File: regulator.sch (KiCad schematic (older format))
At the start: 25 parts, among them IC1 PIC12F675-I/P, Q1 PN2222A, Q2 2N2907A, Q3 BUK9511-55A (Logic Level), Q4 PN2222A, Q5 BUK9511-55A (Logic Level), U1 LM7805

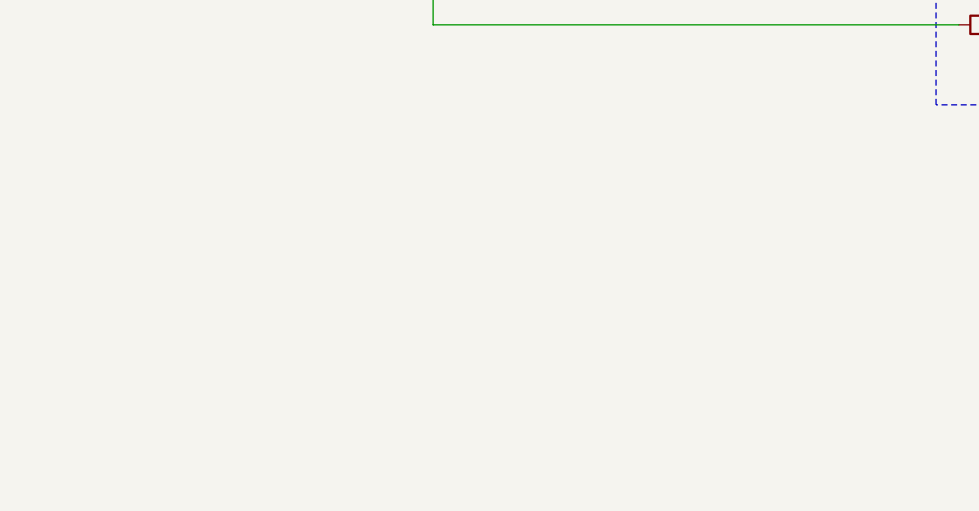
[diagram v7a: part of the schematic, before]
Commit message: Change over voltage reduction parameter. Update Schematic.
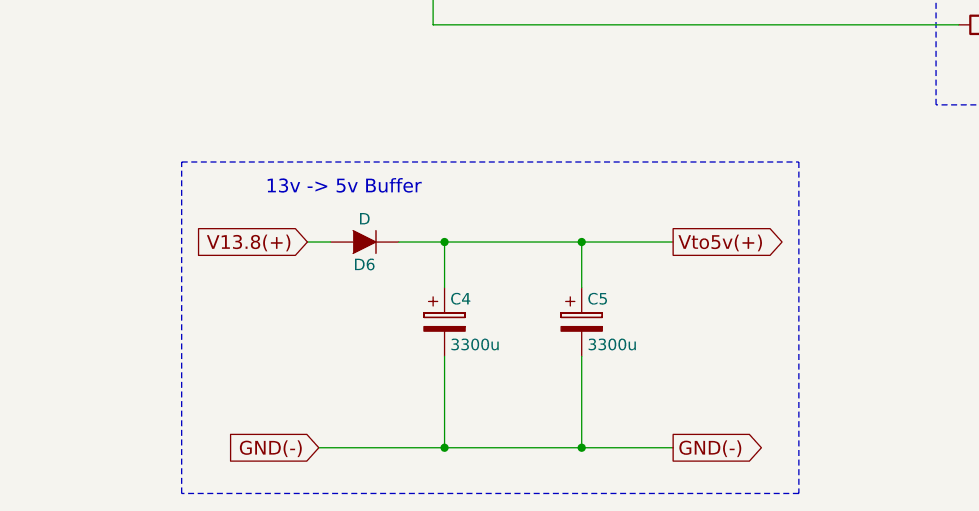
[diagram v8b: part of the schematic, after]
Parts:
- added C4, C5: 3300u, symbol CP
- added D6: D, symbol D
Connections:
- new net GND(-): C4.2, C5.2
- new net V13.8(+): D6.2 (A)
- new net Vto5v(+): C4.1, C5.1, D6.1 (K)
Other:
- note added: "13v -> 5v Buffer"
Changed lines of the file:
@@
 Sheet 1 1
 Title "PWM Regulator v3"
-Date "2015-07-30"
-Rev "1.2j"
+Date "2015-08-03"
+Rev "1.2k"
 Comp ""
 Comment1 ""
@@
 Text Notes 3750 3950 2    60   ~ 0
 GP3 (GND) = 5v\nGP4 (GND) = Check Charging
-Wire Wire Line
-	4800 3700 4800 3900
-Wire Wire Line
-	2250 3700 2250 3350
-Connection ~ 4800 3700
-Connection ~ 4800 1850
-Wire Wire Line
-	6600 3700 6600 2550
-Wire Wire Line
-	6600 2250 6600 1850
-Connection ~ 6600 1850
-Wire Wire Line
-	7400 1850 8650 1850
-Connection ~ 2250 3700
-Wire Wire Line
-	1750 2750 2250 2750
-Wire Wire Line
-	1900 3300 1900 3700
-Connection ~ 1900 3700
-Wire Wire Line
-	7550 1850 7550 2200
-Connection ~ 7550 1850
-Wire Wire Line
-	7550 3700 7550 2500
-Connection ~ 6600 3700
-Wire Wire Line
-	8000 1850 8000 2350
-Connection ~ 8000 1850
-Wire Wire Line
-	8000 2650 8000 2900
-Connection ~ 7550 3700
-Wire Wire Line
-	3850 2750 4050 2750
-Wire Wire Line
-	4450 3400 7750 3400
-Wire Wire Line
-	7750 3400 7750 2800
-Wire Wire Line
-	7750 2800 8000 2800
-Connection ~ 8000 2800
-Wire Wire Line
-	8150 3700 8150 3150
-Connection ~ 8150 3700
-Wire Wire Line
-	5200 2450 5200 3000
-Wire Wire Line
-	3850 2850 4450 2850
-Wire Wire Line
-	4450 2850 4450 3100
-Wire Wire Line
-	4650 2400 4650 2550
-Wire Wire Line
-	4650 2100 4650 2050
-Wire Wire Line
-	4250 2050 6050 2050
-Wire Wire Line
-	4750 2450 4650 2450
-Connection ~ 4650 2450
-Wire Wire Line
-	4650 3700 4650 2950
-Connection ~ 4650 3700
-Wire Wire Line
-	5050 2450 5200 2450
-Connection ~ 5200 2550
-Wire Wire Line
-	6050 2900 6050 3200
-Wire Wire Line
-	5800 2750 5800 2150
-Connection ~ 4650 2050
-Wire Wire Line
-	6050 2050 6050 2600
-Connection ~ 5500 2050
-Wire Wire Line
-	5500 2050 5500 2350
-Wire Wire Line
-	6200 3200 6200 1850
-Connection ~ 6200 1850
-Wire Wire Line
-	1100 3700 8650 3700
-Wire Wire Line
-	1900 2050 1900 3000
-Connection ~ 1900 2750
-Wire Wire Line
-	5500 2750 5500 2800
-Wire Wire Line
-	5500 3200 6200 3200
-Connection ~ 6050 3200
-Wire Wire Line
-	5800 2750 5500 2750
-Wire Wire Line
-	6550 1850 6800 1850
-Wire Wire Line
-	6000 1850 6250 1850
-Wire Wire Line
-	950  1850 950  2750
-Wire Wire Line
-	4800 1500 4800 1850
-Wire Wire Line
-	3900 2950 3850 2950
-Wire Wire Line
-	4200 2950 4250 2950
-Wire Wire Line
-	4250 2950 4250 3250
-Wire Wire Line
-	4250 3650 4250 3700
-Connection ~ 4250 3700
-Wire Wire Line
-	1900 2050 3950 2050
-Wire Wire Line
-	2700 1850 5600 1850
-Wire Wire Line
-	2400 1850 950  1850
-Wire Wire Line
-	1350 1500 4800 1500
-Wire Wire Line
-	3650 2350 3850 2350
-Wire Wire Line
-	3850 2350 3850 3050
-Wire Wire Line
-	3350 2350 3200 2350
-Wire Wire Line
-	3200 2350 3200 2050
-Connection ~ 3200 2050
-Wire Wire Line
-	3850 3250 4000 3250
 $Comp
 L R R7
@@
 	0    -1   -1   0
 $EndComp
-Wire Wire Line
-	6300 4700 4000 4700
-Wire Wire Line
-	4000 4700 4000 3250
 $Comp
 L Q_NMOS_GDS-RESCUE-regulator Q5
@@
 	1    0    0    -1
 $EndComp
-Wire Wire Line
-	6700 4700 6600 4700
-Wire Notes Line
-	8350 4300 8350 5050
-Wire Notes Line
-	8350 5050 6200 5050
-Wire Notes Line
-	6200 5050 6200 4300
-Wire Notes Line
-	6200 4300 8350 4300
 Text Notes 6250 4400 0    60   ~ 0
 Replace D1, PWM Sync
 Text Notes 2600 4250 0    60   ~ 0
 Output 2A -> C2 > 420uF
+$Comp
+L CP C4
+U 1 1 55BEEF2F
+P 4050 6000
+F 0 "C4" H 4075 6100 50  0000 L CNN
+F 1 "3300u" H 4075 5900 50  0000 L CNN
+F 2 "" H 4088 5850 30  0000 C CNN
+F 3 "" H 4050 6000 60  0000 C CNN
+	1    4050 6000
+	1    0    0    -1
+$EndComp
+$Comp
+L CP C5
+U 1 1 55BEF2D6
+P 4650 6000
+F 0 "C5" H 4675 6100 50  0000 L CNN
+F 1 "3300u" H 4675 5900 50  0000 L CNN
+F 2 "" H 4688 5850 30  0000 C CNN
+F 3 "" H 4650 6000 60  0000 C CNN
+	1    4650 6000
+	1    0    0    -1
+$EndComp
+$Comp
+L D D6
+U 1 1 55BEF35E
+P 3700 5650
+F 0 "D6" H 3700 5750 50  0000 C CNN
+F 1 "D" H 3700 5550 50  0000 C CNN
+F 2 "" H 3700 5650 60  0000 C CNN
+F 3 "" H 3700 5650 60  0000 C CNN
+	1    3700 5650
+	-1   0    0    1
+$EndComp
+Text GLabel 3450 5650 0    60   Input ~ 0
+V13.8(+)
+Text GLabel 3500 6550 0    60   Input ~ 0
+GND(-)
+Text GLabel 5050 6550 2    60   Output ~ 0
+GND(-)
+Text GLabel 5050 5650 2    60   Output ~ 0
+Vto5v(+)
+Wire Wire Line
+	4800 3700 4800 3900
+Wire Wire Line
+	2250 3700 2250 3350
+Connection ~ 4800 3700
+Connection ~ 4800 1850
+Wire Wire Line
+	6600 3700 6600 2550
+Wire Wire Line
+	6600 2250 6600 1850
+Connection ~ 6600 1850
+Wire Wire Line
+	7400 1850 8650 1850
+Connection ~ 2250 3700
+Wire Wire Line
+	1750 2750 2250 2750
+Wire Wire Line
+	1900 3300 1900 3700
+Connection ~ 1900 3700
+Wire Wire Line
+	7550 1850 7550 2200
+Connection ~ 7550 1850
+Wire Wire Line
+	7550 3700 7550 2500
+Connection ~ 6600 3700
+Wire Wire Line
+	8000 1850 8000 2350
+Connection ~ 8000 1850
+Wire Wire Line
+	8000 2650 8000 2900
+Connection ~ 7550 3700
+Wire Wire Line
+	3850 2750 4050 2750
+Wire Wire Line
+	4450 3400 7750 3400
+Wire Wire Line
+	7750 3400 7750 2800
+Wire Wire Line
+	7750 2800 8000 2800
+Connection ~ 8000 2800
+Wire Wire Line
+	8150 3700 8150 3150
+Connection ~ 8150 3700
+Wire Wire Line
+	5200 2450 5200 3000
+Wire Wire Line
+	3850 2850 4450 2850
+Wire Wire Line
+	4450 2850 4450 3100
+Wire Wire Line
+	4650 2400 4650 2550
+Wire Wire Line
+	4650 2100 4650 2050
+Wire Wire Line
+	4250 2050 6050 2050
+Wire Wire Line
+	4750 2450 4650 2450
+Connection ~ 4650 2450
+Wire Wire Line
+	4650 3700 4650 2950
+Connection ~ 4650 3700
+Wire Wire Line
+	5050 2450 5200 2450
+Connection ~ 5200 2550
+Wire Wire Line
+	6050 2900 6050 3200
+Wire Wire Line
+	5800 2750 5800 2150
+Connection ~ 4650 2050
+Wire Wire Line
+	6050 2050 6050 2600
+Connection ~ 5500 2050
+Wire Wire Line
+	5500 2050 5500 2350
+Wire Wire Line
+	6200 3200 6200 1850
+Connection ~ 6200 1850
+Wire Wire Line
+	1100 3700 8650 3700
+Wire Wire Line
+	1900 2050 1900 3000
+Connection ~ 1900 2750
+Wire Wire Line
+	5500 2750 5500 2800
+Wire Wire Line
+	5500 3200 6200 3200
+Connection ~ 6050 3200
+Wire Wire Line
+	5800 2750 5500 2750
+Wire Wire Line
+	6550 1850 6800 1850
+Wire Wire Line
+	6000 1850 6250 1850
+Wire Wire Line
+	950  1850 950  2750
+Wire Wire Line
+	4800 1500 4800 1850
+Wire Wire Line
+	3900 2950 3850 2950
+Wire Wire Line
+	4200 2950 4250 2950
+Wire Wire Line
+	4250 2950 4250 3250
+Wire Wire Line
+	4250 3650 4250 3700
+Connection ~ 4250 3700
+Wire Wire Line
+	1900 2050 3950 2050
+Wire Wire Line
+	2700 1850 5600 1850
+Wire Wire Line
+	2400 1850 950  1850
+Wire Wire Line
+	1350 1500 4800 1500
+Wire Wire Line
+	3650 2350 3850 2350
+Wire Wire Line
+	3850 2350 3850 3050
+Wire Wire Line
+	3350 2350 3200 2350
+Wire Wire Line
+	3200 2350 3200 2050
+Connection ~ 3200 2050
+Wire Wire Line
+	3850 3250 4000 3250
+Wire Wire Line
+	6300 4700 4000 4700
+Wire Wire Line
+	4000 4700 4000 3250
+Wire Wire Line
+	6700 4700 6600 4700
+Wire Notes Line
+	8350 4300 8350 5050
+Wire Notes Line
+	8350 5050 6200 5050
+Wire Notes Line
+	6200 5050 6200 4300
+Wire Notes Line
+	6200 4300 8350 4300
+Wire Wire Line
+	3450 5650 3550 5650
+Wire Wire Line
+	3850 5650 5050 5650
+Wire Wire Line
+	3500 6550 5050 6550
+Wire Wire Line
+	4050 6150 4050 6550
+Connection ~ 4050 6550
+Wire Wire Line
+	4050 5850 4050 5650
+Connection ~ 4050 5650
+Wire Wire Line
+	4650 6150 4650 6550
+Connection ~ 4650 6550
+Wire Wire Line
+	4650 5850 4650 5650
+Connection ~ 4650 5650
+Text Notes 3950 5450 2    60   ~ 0
+13v -> 5v Buffer
+Wire Notes Line
+	2900 5300 5600 5300
+Wire Notes Line
+	5600 5300 5600 6750
+Wire Notes Line
+	5600 6750 2900 6750
+Wire Notes Line
+	2900 6750 2900 5300
 $EndSCHEMATC
